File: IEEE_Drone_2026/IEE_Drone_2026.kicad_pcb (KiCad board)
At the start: 4 copper layers, 30 x 60 mm, 47 parts, among them IC1 TPSM84209RKHT, J1 ESC, J10 M2, J11 Conn_01x02_Socket, J13 USB_C_Receptacle_USB2.0_16P, J6 Pixy2, J7 M2, J8 M2, J9 M2, Q1 2N2222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

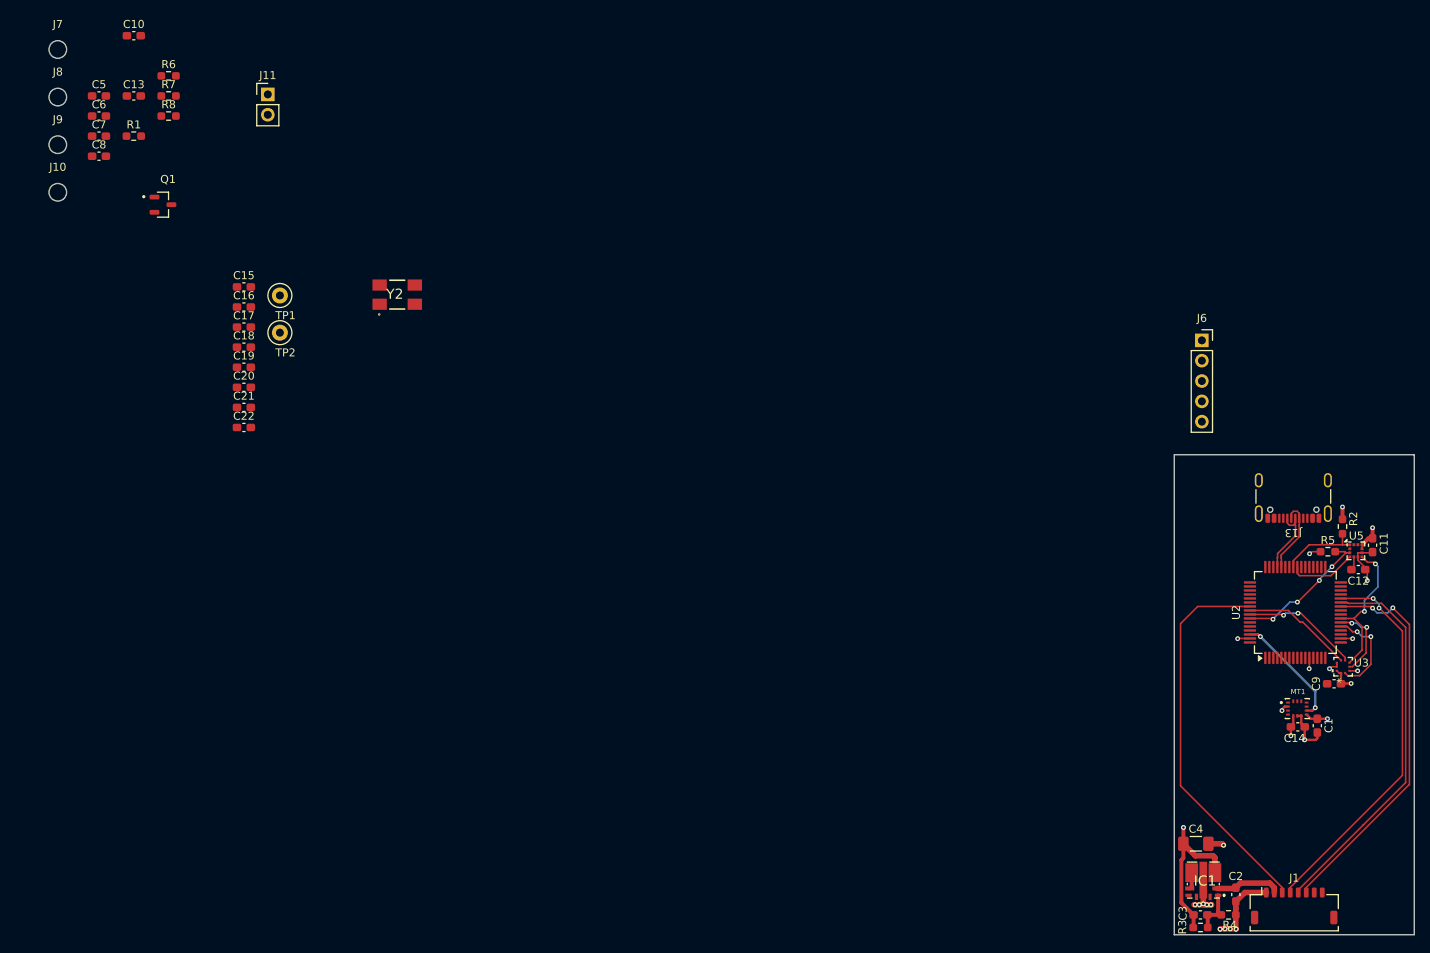
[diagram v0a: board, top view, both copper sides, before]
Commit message: some routing updates
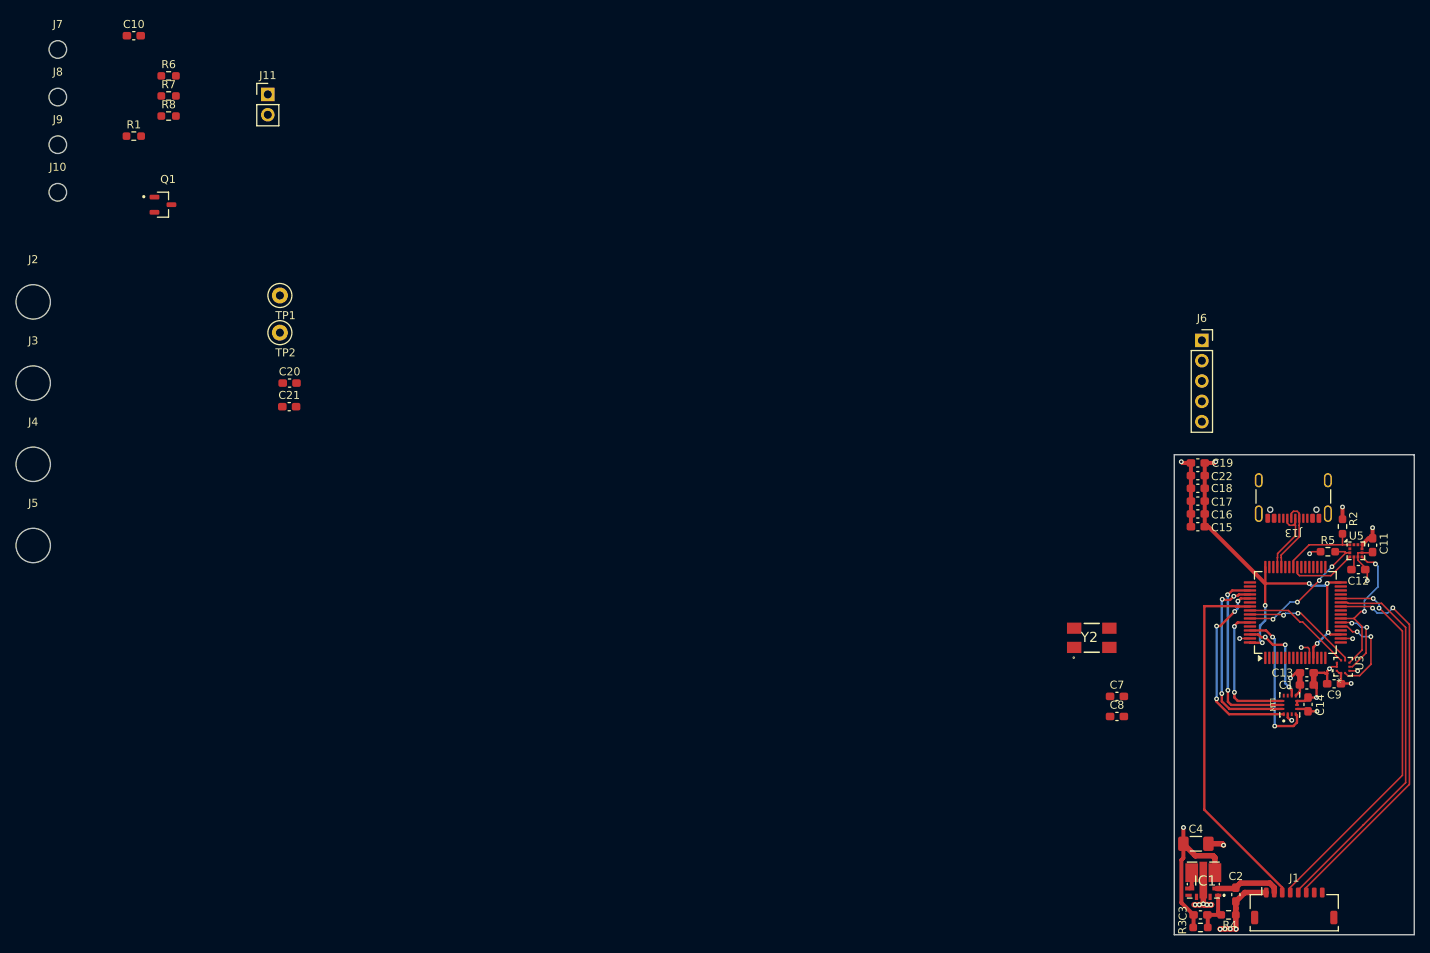
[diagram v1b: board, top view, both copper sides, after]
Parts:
- removed C5, C6: 22pF, Capacitor_SMD:C_0603_1608Metric_Pad1.08x0.95mm_HandSolder
- added J2: M4 Mounting, Mounting:MountingHole_4.3mm_M4, F.Cu at (34.0, 56.3)
- added J3: M4 Mounting, Mounting:MountingHole_4.3mm_M4, F.Cu at (34.0, 66.5)
- added J4: M4 Mounting, Mounting:MountingHole_4.3mm_M4, F.Cu at (34.0, 76.6)
- added J5: M4 Mounting, Mounting:MountingHole_4.3mm_M4, F.Cu at (34.0, 86.8)
- moved C13 163.4 mm to (193.2, 102.7)
- moved C7 145.2 mm to (169.5, 105.6)
- moved C8 145.2 mm to (169.5, 108.1)
- moved C15 123.0 mm to (179.6, 84.4), turned to 180 degrees
- moved C16 122.0 mm to (179.6, 82.8), turned to 180 degrees
- moved C17 121.2 mm to (179.6, 81.2), turned to 180 degrees
- moved C18 120.5 mm to (179.6, 79.6), turned to 180 degrees
- moved C19 119.8 mm to (179.6, 76.4), turned to 180 degrees
- moved C22 119.4 mm to (179.6, 78.0), turned to 180 degrees
- moved Y2 96.8 mm to (166.3, 98.3)
- moved C20 5.74 mm to (66.0, 66.5)
- moved C21 5.66 mm to (66.0, 69.4)
- moved C1 5.26 mm to (193.2, 104.2), turned to 0 degrees
- moved C14 3.08 mm to (193.4, 106.6), turned to -90 degrees
- moved MT1 1.05 mm to (191.1, 106.7), turned to 90 degrees
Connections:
- C15 pad 1: Net-(U2-VBAT) -> +3.3V
- C16 pad 1: Net-(U2-VBAT) -> +3.3V
- C17 pad 1: Net-(U2-VBAT) -> +3.3V
- C18 pad 1: Net-(U2-VBAT) -> +3.3V
- C19 pad 1: Net-(U2-VBAT) -> +3.3V
- C22 pad 1: Net-(U2-VBAT) -> +3.3V
- U2 pad 1: Net-(U2-VBAT) -> unconnected-(U2-VBAT-Pad1)
- U2 pad 13: Net-(U2-VBAT) -> +3.3V
- U2 pad 19: Net-(U2-VBAT) -> +3.3V
- U2 pad 32: Net-(U2-VBAT) -> +3.3V
- U2 pad 48: Net-(U2-VBAT) -> +3.3V
- U2 pad 64: Net-(U2-VBAT) -> +3.3V
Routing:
- net +3.3V: track 34.9 -> 89.5 mm, vias 7 -> 14
- net /MISO (SPI3): track 0.00 -> 24.6 mm, vias 0 -> 3
- net /MOSI (SPI3): track 0.00 -> 24.6 mm, vias 0 -> 4
- net /SCK (SPI3): track 0.00 -> 23.4 mm, vias 0 -> 2
- net /PB8: track 0.00 -> 18.5 mm, vias 0 -> 2
- net /PB7: track 0.00 -> 17.3 mm, vias 0 -> 2
- net GND: track 37.5 -> 51.4 mm, vias 18 -> 19
- net /PB9: track 14.4 -> 11.7 mm, vias 2 -> 3
- net /PB3: track 48.4 -> 46.2 mm

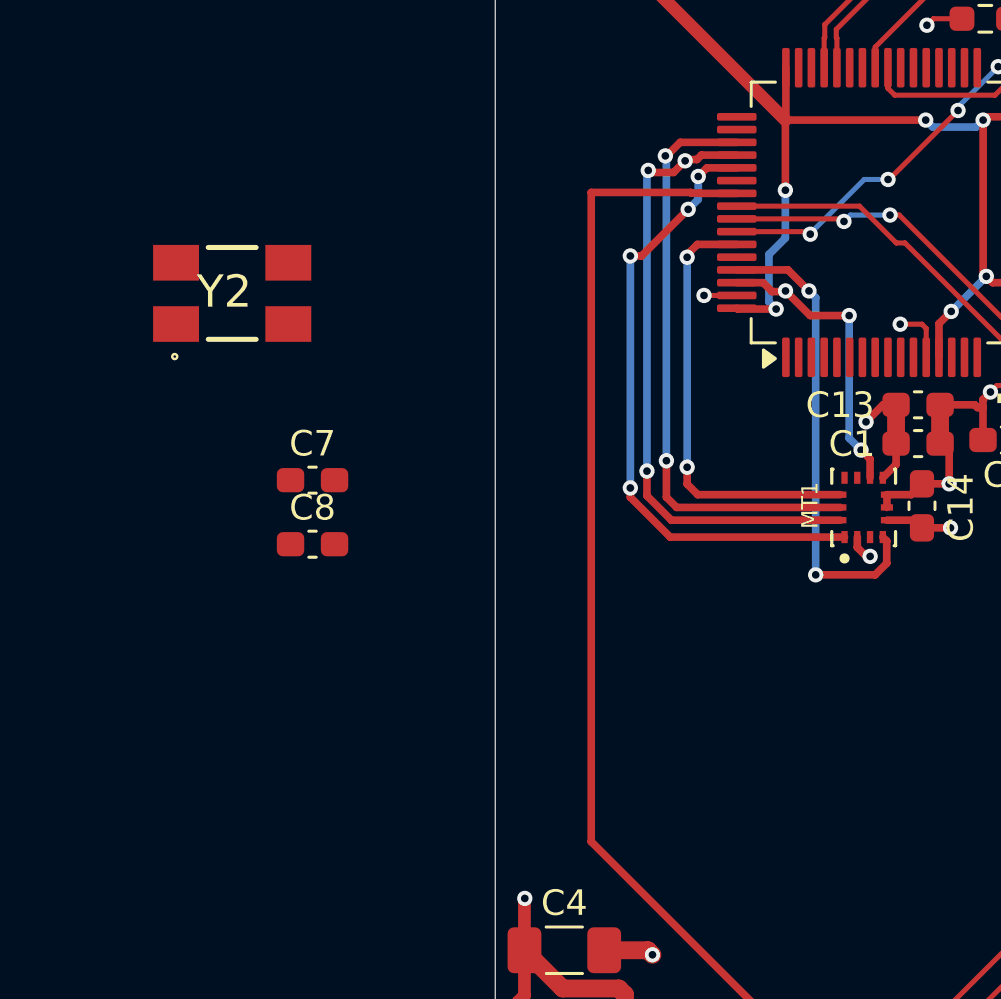
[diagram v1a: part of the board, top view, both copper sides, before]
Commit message: routed more things
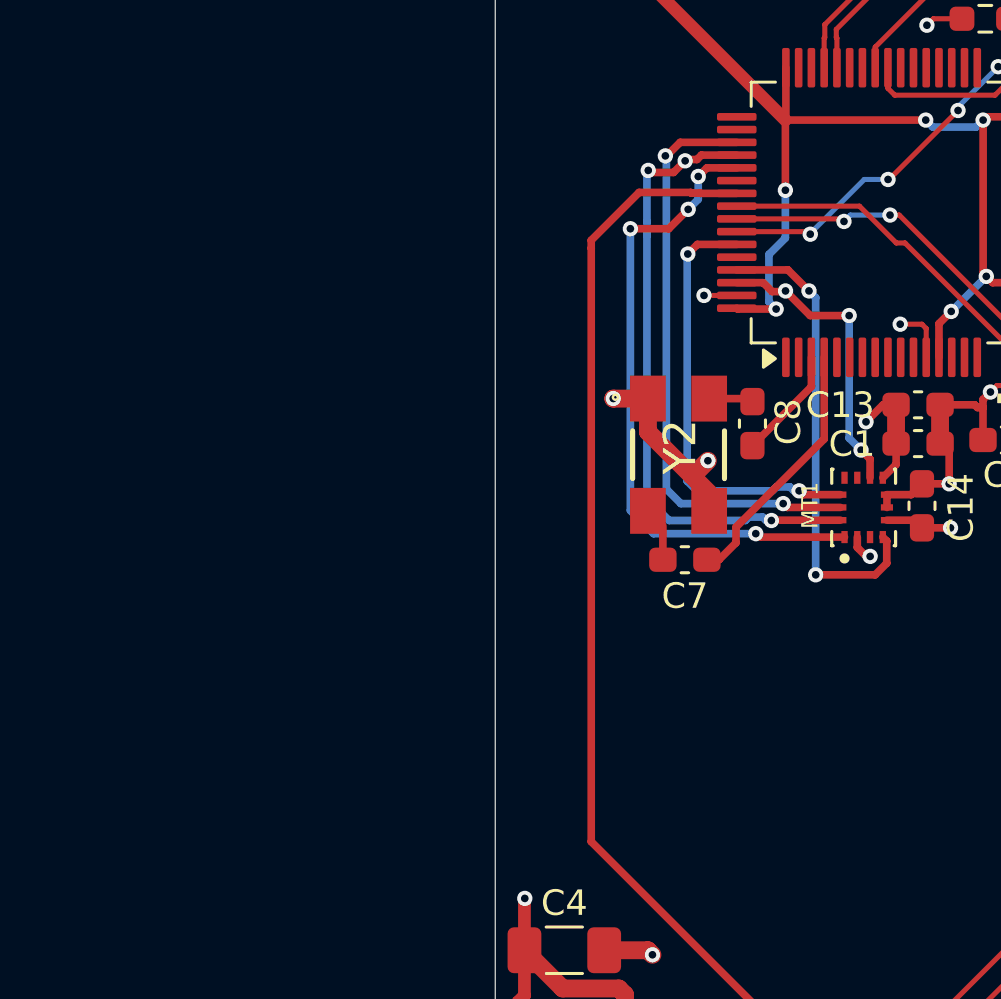
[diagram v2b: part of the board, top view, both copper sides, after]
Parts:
- moved Y2 18.6 mm to (183.8, 104.6), turned to -90 degrees
- moved C8 17.9 mm to (186.7, 103.4), turned to -90 degrees
- moved C7 14.9 mm to (184.1, 108.7)
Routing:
- net Net-(U2-PC15): track 0.00 -> 10.1 mm
- net GND: track 51.4 -> 58.3 mm, vias 19 -> 21
- net Net-(U2-PC14): track 0.00 -> 4.42 mm
- net Net-(Y2-GND_2): track 0.00 -> 1.58 mm
- net Net-(Y2-GND_1): track 0.00 -> 1.33 mm
- net /PB3: track 46.2 -> 45.1 mm
- net /MOSI (SPI3): track 24.6 -> 25.7 mm

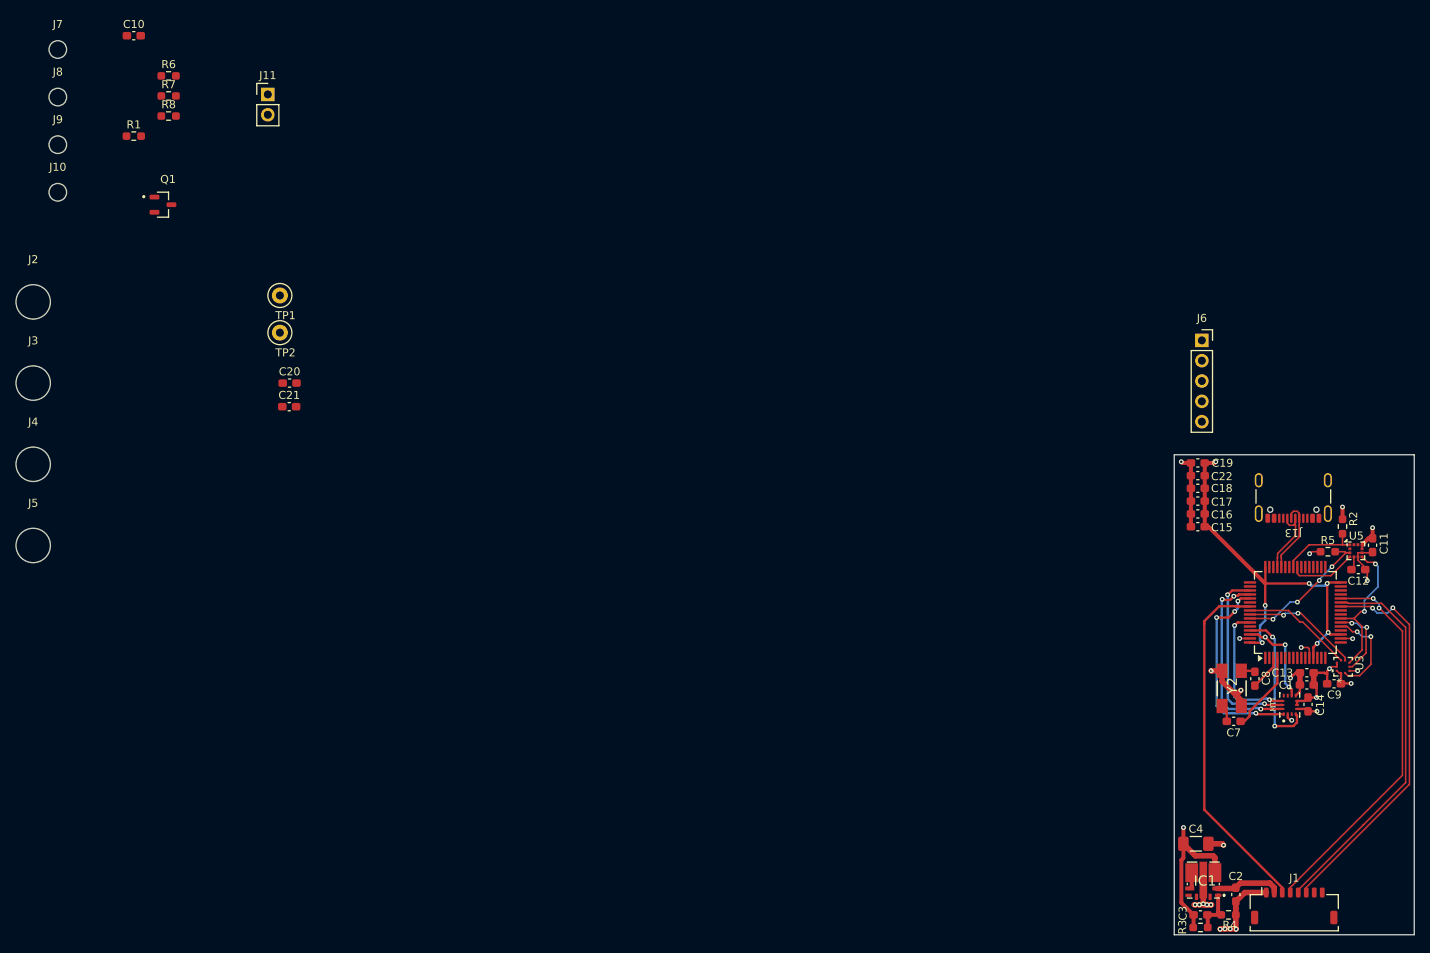
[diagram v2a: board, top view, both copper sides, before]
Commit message: new dimensions for board
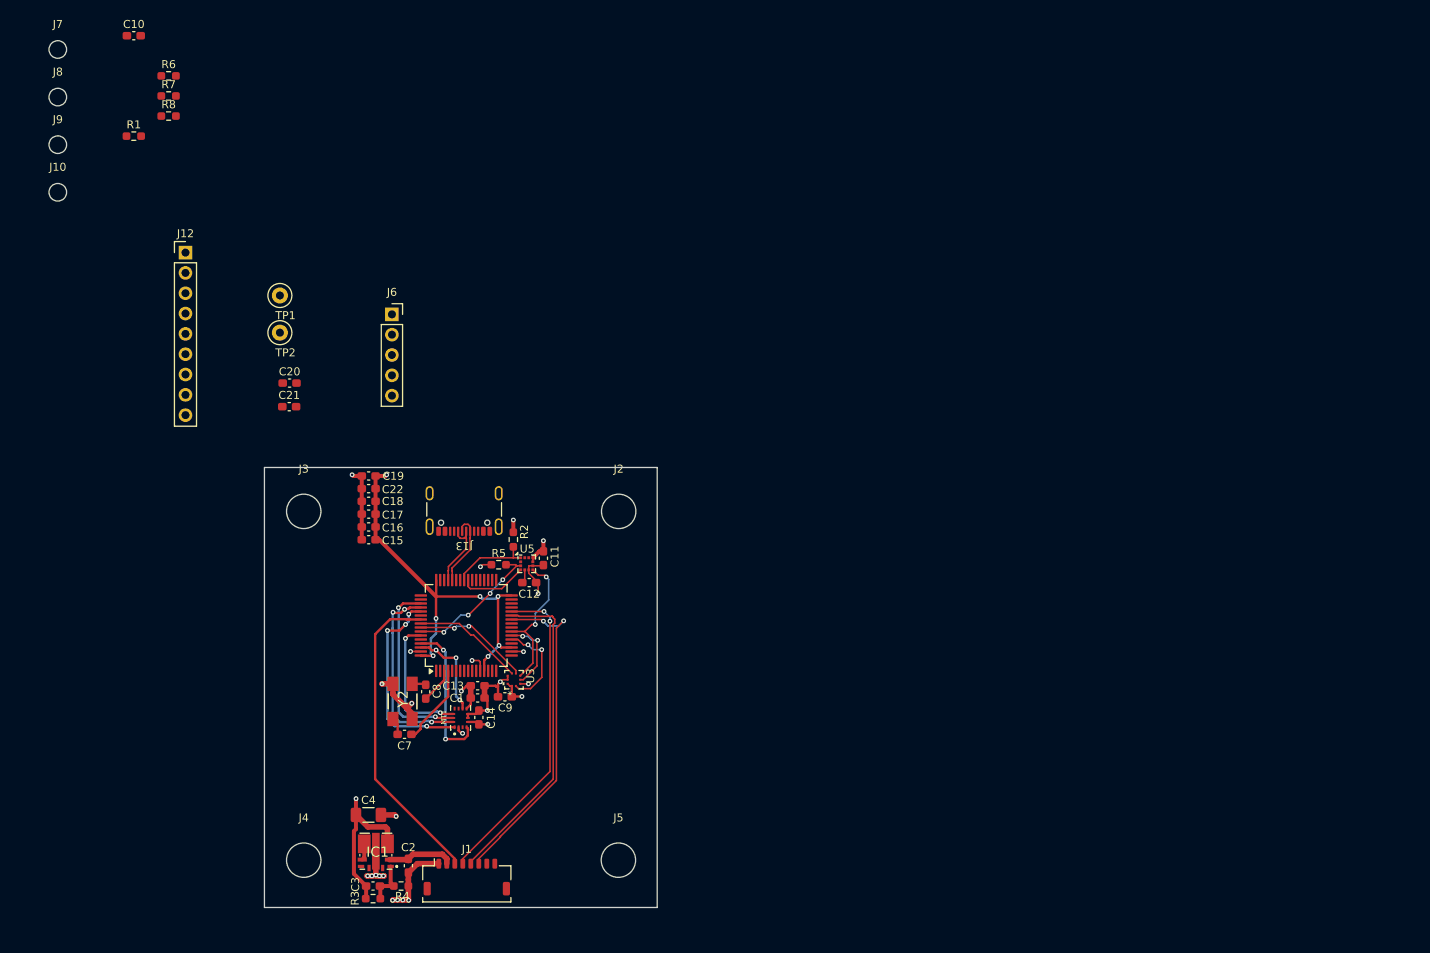
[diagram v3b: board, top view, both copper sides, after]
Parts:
- removed J11: Conn_01x02_Socket, Connector_PinHeader_2.54mm:PinHeader_1x02_P2.54mm_Vertical
- removed Q1: 2N2222, 2n2222:SOT95P237X111-3N
- added J12: RF, Connector_PinHeader_2.54mm:PinHeader_1x09_P2.54mm_Vertical, F.Cu at (53.0, 50.1)
- moved C12 103.7 mm to (96.0, 91.4)
- moved C8 103.7 mm to (83.1, 105.0)
- moved C9 103.7 mm to (93.0, 105.7)
- moved MT1 103.7 mm to (87.4, 108.3)
- moved R2 103.7 mm to (94.0, 86.0)
- moved R5 103.7 mm to (92.2, 89.2)
- moved U2 103.7 mm to (88.1, 96.8)
- moved U3 103.7 mm to (94.1, 103.5)
- moved Y2 103.7 mm to (80.2, 106.2)
- moved C1 103.7 mm to (89.6, 105.8)
- moved C11 103.7 mm to (97.8, 88.3)
- moved C13 103.7 mm to (89.6, 104.3)
- moved C14 103.7 mm to (89.7, 108.2)
- moved C15 103.7 mm to (75.9, 86.0)
- moved C16 103.7 mm to (75.9, 84.4)
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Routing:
- net /PB2: track 48.2 -> 40.5 mm
- net /PB1: track 48.2 -> 41.0 mm
- net /PB0: track 48.9 -> 41.9 mm
- net /PB3: track 45.1 -> 39.9 mm
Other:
- board size 30 x 60 mm -> 49.1 x 55 mm

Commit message: completely updated design
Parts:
- moved R2 4.89 mm to (95.4, 90.7)
- moved C1 4.89 mm to (91.0, 110.5)
- moved C14 4.89 mm to (91.1, 112.9)
- moved C18 4.89 mm to (77.4, 85.9)
- moved C8 4.89 mm to (84.5, 109.7)
- moved U5 4.89 mm to (97.1, 93.7)
- moved Y2 4.89 mm to (81.6, 110.9)
- moved C12 4.89 mm to (97.4, 96.1)
- moved C9 4.89 mm to (94.4, 110.3)
- moved J13 4.89 mm to (89.3, 86.0)
- moved R5 4.89 mm to (93.6, 93.8)
- moved U3 4.89 mm to (95.5, 108.2)
- moved C11 4.89 mm to (99.2, 93.0)
- moved C13 4.89 mm to (91.0, 109.0)
- moved C15 4.89 mm to (77.4, 90.7)
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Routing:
- net /PB0: track 41.9 -> 36.9 mm
- net /PB2: track 40.5 -> 35.5 mm
- net /PB1: track 41.0 -> 36.1 mm
- net /PB3: track 39.9 -> 44.4 mm
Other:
- board size 49.1 x 55 mm -> 49 x 49.5 mm
